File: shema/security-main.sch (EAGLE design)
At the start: 22 parts, among them Q1 IRF520, Q2 FDN360P, T1 2N706, T2 2N706

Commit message: shema changed
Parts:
- removed T1, T2: 2N706, transistor:2N706
- added C3, C4, C5: (no value), capacitor-wima:C2,5-3
- added D4: MBRA340T3, diode:MBRA340T3
- added JP1: (no value), pinhead:PINHD-1X2/90
- added JP2: (no value), adafruit:PINHD-1X8BIG
- added Q3, Q4: AP3310GH, transistor-power:FDN360P
- added SV1: (no value), con-lstb:MA08-1
- renumbered U1 to PIC16F690
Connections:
- removed net N$11: SG1.-, T2.C
- removed net N$4: PIC16F690.RB6/SCK/SCL
- new net DOOR_BUTTON: C4.1, D4.A, PIC16F690.RB6/SCK/SCL
- new net N$1: D4.C, X1-3.KL
- new net N$2: Q4.D, SG1.+
- net DOOR: now also C3.1, Q3.D; no longer T1.E
- net GND: now also C3.2, C4.2, C5.2, JP1.2, SG1.-; no longer T2.E
- net KEYPAD_COL1: now also JP2.5, SV1.5
- net KEYPAD_COL2: now also JP2.6, SV1.6
- net KEYPAD_COL3: now also JP2.7, SV1.7
- net KEYPAD_COL4: now also JP2.8, SV1.8
- net KEYPAD_ROW1: now also JP2.1, SV1.1
- net KEYPAD_ROW2: now also JP2.2, SV1.2
- net KEYPAD_ROW3: now also JP2.3, SV1.3
- net KEYPAD_ROW4: now also JP2.4, SV1.4
- net N$12: now also Q3.G; no longer T1.B
- net N$3: now also Q4.G; no longer T2.B
- net V+: now also C5.1, JP1.1, Q3.S, Q4.S; no longer SG1.+, T1.C
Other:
- moved on the sheet: C1, C2, KEYPAD4X4, LED1, LED2, Q1, Q2, R1, R2, R3, R4, SG1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

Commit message: sheme changes
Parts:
- removed Q3, Q4: AP3310GH, transistor-power:FDN360P
- removed X2: (no value), con-ptr500:AK300/3
- removed X3: (no value), con-ptr500:AK300/5
- removed X4: (no value), con-ptr500:AK300/2
- added C6: 0.1, capacitor-wima:C2,5-3
- added C7: 1500x6.3, rcl:CPOL-EU153CLV-0505
- added C8: 0.047, capacitor-wima:C2,5-3
- added D5: MBRA340T3, diode:MBRA340T3
- added JP3: PICkit2, pinhead:PINHD-1X5
- added JP4: SPI, pinhead:PINHD-1X4
- added JP5: RS-232, adafruit:PINHD-1X3
- added R5, R6: 10k, resistor:R-EU_0204/2V
- added S1, S2: RDT1034, switch:RDT1034
- C1, C2, C3, C4: value (none) -> 10n
- C5: value (none) -> 0.1
- JP1: value (none) -> POWER
- JP2: device adafruit:PINHD-1X8BIG -> adafruit:PINHD-1X8CLEANBIG
- LED1: value W49180 -> FLY-5013GD
- LED2: value W49180 -> FLY-5013SRD
- PIC16F690: value (none) -> CPU
- Q1: value IRF520 -> 70TO3GH; device transistor-power:IRF520 -> adafruit:MOSFET-NREFLOW
- Q2: value FDN360P -> 2N4403; device transistor-power:FDN360P -> transistor-pnp:MPSA56-TO92
- R1, R4: value (none) -> 1K
- R2, R3: value (none) -> 1k
- SG1: value EB2209A -> KPX-1205A
- SV1: value (none) -> KEYPAD
- X1: value (none) -> DOOR-SENSORS
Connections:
- net N$1 renamed DOOR_BUTTON-1
- net N$5 renamed DOOR-1
- net N$6 renamed LOOK2-1
- net N$7 renamed LOOK1-1
- removed net KEYPAD_COL4: JP2.8, KEYPAD4X4.C4, PIC16F690.RA3/MCLR/VPP, SV1.8
- removed net KEYPAD_ROW4: JP2.4, KEYPAD4X4.R4, PIC16F690.AN7/RC3, SV1.4
- removed net LOOK1: C1.1, D1.A, PIC16F690.RA4/AN3/T1GI/OSC2
- removed net LOOK2: C2.1, D2.A, PIC16F690.RA5/T1CKI/OSC1
- removed net N$3 (its old number): Q4.G, R2.2
- new net ICSPCLK: JP3.5
- new net ICSPDAT: JP3.4
- new net KEYPAD_COL1-1: JP2.4, KEYPAD4X4.C1
- new net KEYPAD_COL2-1: JP2.3, KEYPAD4X4.C2
- new net KEYPAD_COL3-1: JP2.2, KEYPAD4X4.C3
- new net KEYPAD_COL4-1: JP2.1, KEYPAD4X4.C4
- new net KEYPAD_ROW1-1: JP2.8, KEYPAD4X4.R1
- new net KEYPAD_ROW2-1: JP2.7, KEYPAD4X4.R2
- new net KEYPAD_ROW3-1: JP2.6, KEYPAD4X4.R3
- new net KEYPAD_ROW4-1: JP2.5, KEYPAD4X4.R4
- new net LOOCK1: C3.1, D1.A, PIC16F690.RA4/AN3/T1GI/OSC2
- new net LOOCK2: C1.1, D2.A, PIC16F690.RA5/T1CKI/OSC1
- new net N$1: Q1.G, R2.2
- new net N$4: D5.A, JP1.1
- new net RESET: PIC16F690.RA3/MCLR/VPP, S2.B
- new net SCK: JP4.3, PIC16F690.RB6/SCK/SCL
- new net SDI: JP4.1, PIC16F690.RB4/AN10/SDI/SDO
- new net SDO: JP4.2, PIC16F690.AN9/RC7
- new net VDD_TARGET: JP3.2
- new net VPP: JP3.1
- new net VSS_GROUND: JP3.3
- net BUZ: now also PIC16F690.RC4; no longer PIC16F690.RC5
- net DOOR: now also C4.1, PIC16F690.AN7/RC3, R5.1; no longer C3.1, PIC16F690.RB4/AN10/SDI/SDO, Q3.D, X1-5.KL
- net DOOR-LEDS: now also PIC16F690.RC5; no longer PIC16F690.RC4
- net DOOR_BUTTON: now also C2.1, PIC16F690.AN8/RC6, R6.1, S1.B; no longer C4.1, PIC16F690.RB6/SCK/SCL
- net GND: now also C6.2, C7.-, C8.1, JP4.4, JP5.3, Q1.S, S1.A1, S2.A1; no longer SG1.-, X2-3.KL, X4-1.KL
- net KEYPAD_COL1: no longer JP2.5, KEYPAD4X4.C1
- net KEYPAD_COL2: no longer JP2.6, KEYPAD4X4.C2
- net KEYPAD_COL3: no longer JP2.7, KEYPAD4X4.C3
- net KEYPAD_ROW1: no longer JP2.1, KEYPAD4X4.R1
- net KEYPAD_ROW2: no longer JP2.2, KEYPAD4X4.R2
- net KEYPAD_ROW3: no longer JP2.3, KEYPAD4X4.R3
- net LED-SYS1: now also R1.1; no longer PIC16F690.AN8/RC6, R4.1
- net LED-SYS2: now also Q2.C, R4.1, X1-5.KL; no longer PIC16F690.AN9/RC7, R1.1
- net N$12: now also Q2.B; no longer Q3.G
- net N$2: now also Q1.D, SG1.-; no longer Q4.D, SG1.+
- net RX: now also JP5.1; no longer X2-1.KL
- net TX: now also JP5.2; no longer X2-2.KL
- net V+: now also C6.1, C7.+, C8.2, D5.C, Q2.E, R5.2, R6.2, SG1.+; no longer JP1.1, Q3.S, Q4.S, X4-2.KL
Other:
- note added: "DOOR"
- note added: "DOOR BUTTON"
- note added: "DOOR LEDS"
- note added: "GND"
- note added: "LOOK1"
- note added: "LOOK2"
- moved on the sheet: C1, C2, C3, C4, C5, JP1, JP2, LED1, LED2, R1, R2, R4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

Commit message: changed sheme
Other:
- note added: "LOOCK1"
- note added: "LOOCK2"
- note added: "Security Alarm https://github.com/lexxai/SecurityAlarm http://lexxai.pp.ua 2017"
- note removed: "LOOK1"
- note removed: "LOOK2"
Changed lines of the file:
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@@
 <sheet>
 <plain>
-<text x="-34.798" y="34.798" size="1.778" layer="91">LOOK1</text>
-<text x="-34.798" y="29.972" size="1.778" layer="91">LOOK2</text>
+<text x="-34.798" y="34.798" size="1.778" layer="91">LOOCK1</text>
+<text x="-34.798" y="29.972" size="1.778" layer="91">LOOCK2</text>
 <text x="-27.178" y="19.558" size="1.778" layer="91" align="bottom-right">DOOR</text>
 <text x="-27.178" y="14.478" size="1.778" layer="91" align="bottom-right">DOOR LEDS</text>
 <text x="-27.178" y="24.892" size="1.778" layer="91" align="bottom-right">DOOR BUTTON</text>
 <text x="-27.178" y="9.652" size="1.778" layer="91" align="bottom-right">GND</text>
+<text x="99.06" y="101.6" size="1.778" layer="91">Security Alarm
+https://github.com/lexxai/SecurityAlarm
+http://lexxai.pp.ua
+2017</text>
 </plain>
 <instances>
@@
 </segment>
 </net>
+<net name="N$5" class="0">
+<segment>
+<wire x1="96.52" y1="114.3" x2="96.52" y2="99.06" width="0.1524" layer="91"/>
+<wire x1="96.52" y1="99.06" x2="144.78" y2="99.06" width="0.1524" layer="91"/>
+<wire x1="144.78" y1="99.06" x2="144.78" y2="114.3" width="0.1524" layer="91"/>
+<wire x1="144.78" y1="114.3" x2="96.52" y2="114.3" width="0.1524" layer="91"/>
+</segment>
+</net>
+<net name="N$6" class="0">
+<segment>
+<wire x1="-45.72" y1="124.46" x2="-45.72" y2="-25.4" width="0.1524" layer="91"/>
+<wire x1="-45.72" y1="-25.4" x2="190.5" y2="-25.4" width="0.1524" layer="91"/>
+<wire x1="190.5" y1="-25.4" x2="190.5" y2="124.46" width="0.1524" layer="91"/>
+<wire x1="190.5" y1="124.46" x2="-45.72" y2="124.46" width="0.1524" layer="91"/>
+</segment>
+</net>
 </nets>
 </sheet>
@@
 </schematic>
 </drawing>
+<compatibility>
+<note version="6.3" minversion="6.2.2" severity="warning">
+Since Version 6.2.2 text objects can contain more than one line,
+which will not be processed correctly with this version.
+</note>
+</compatibility>
 </eagle>

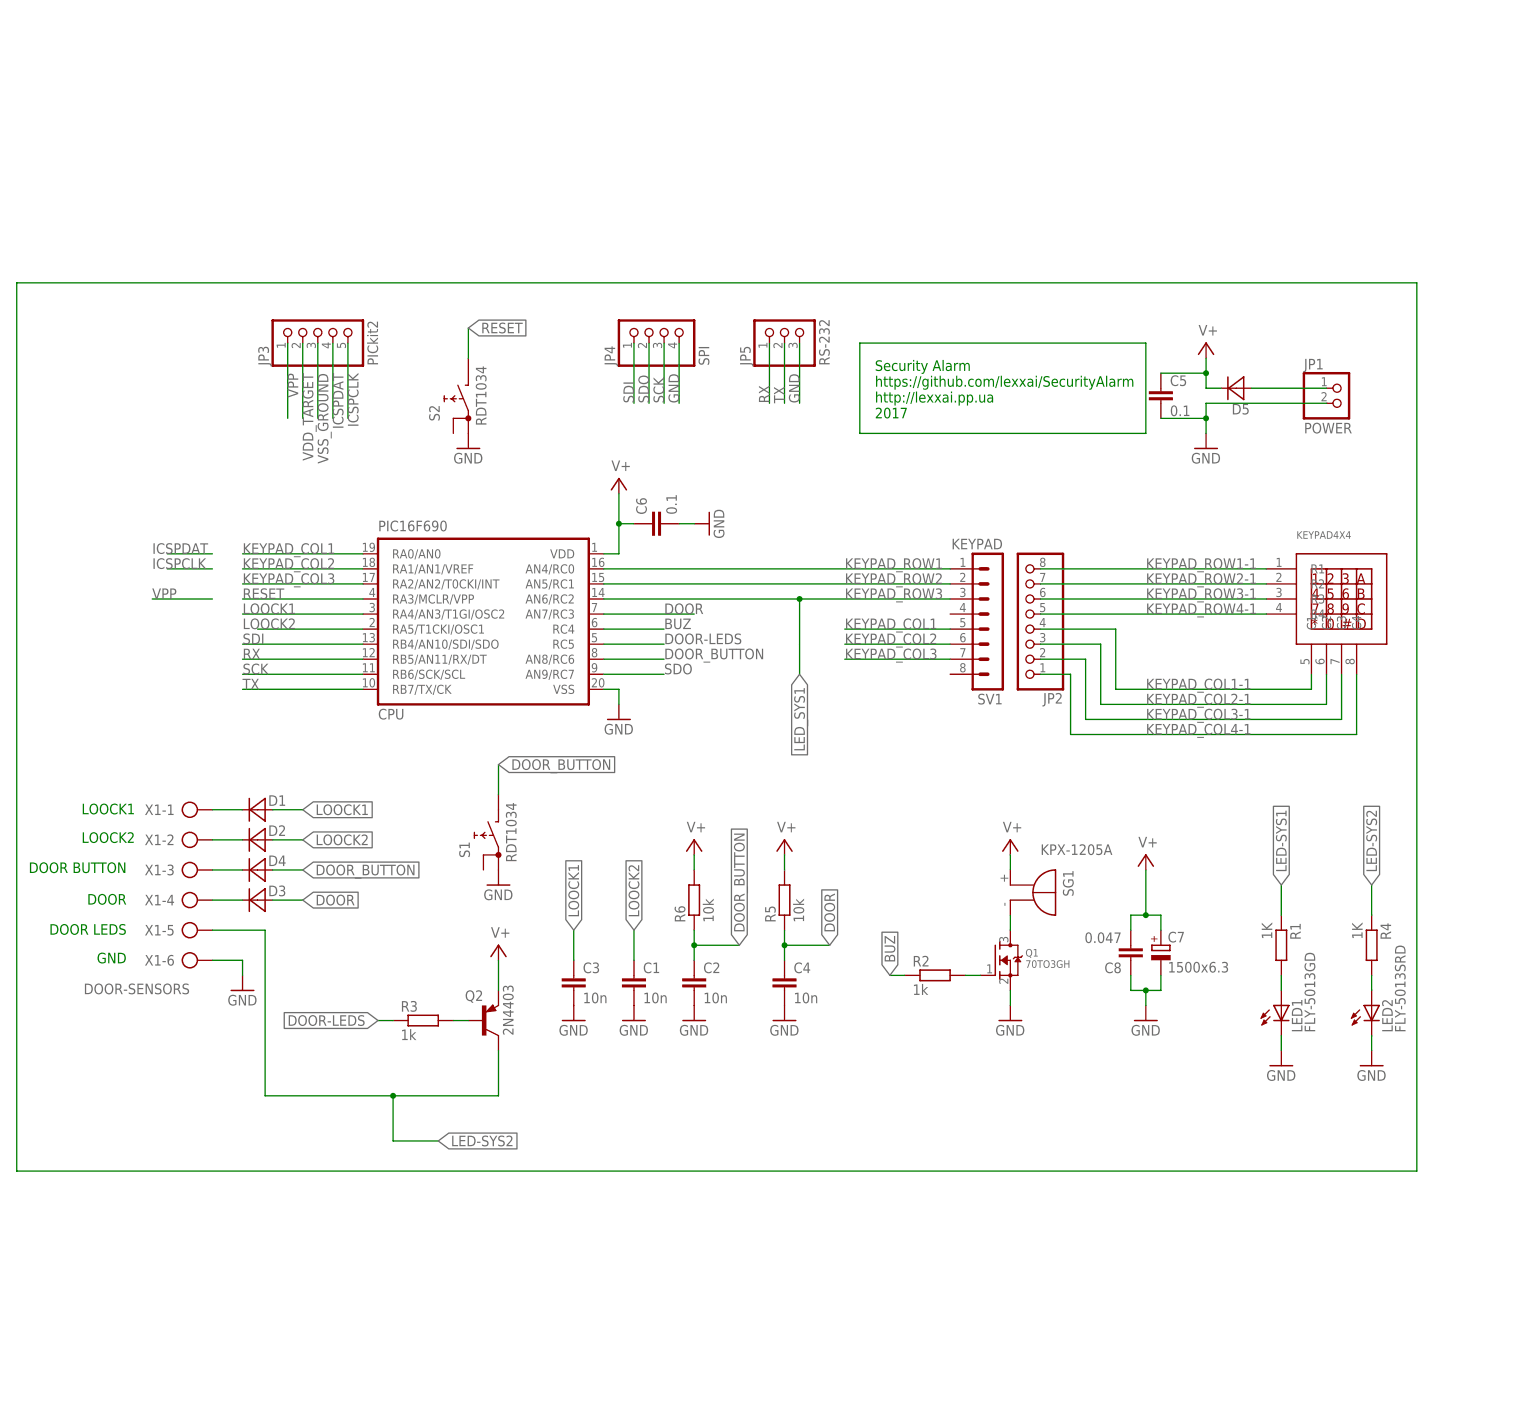
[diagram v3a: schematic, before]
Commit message: 1wire lib added , not tested shema changes: power supply
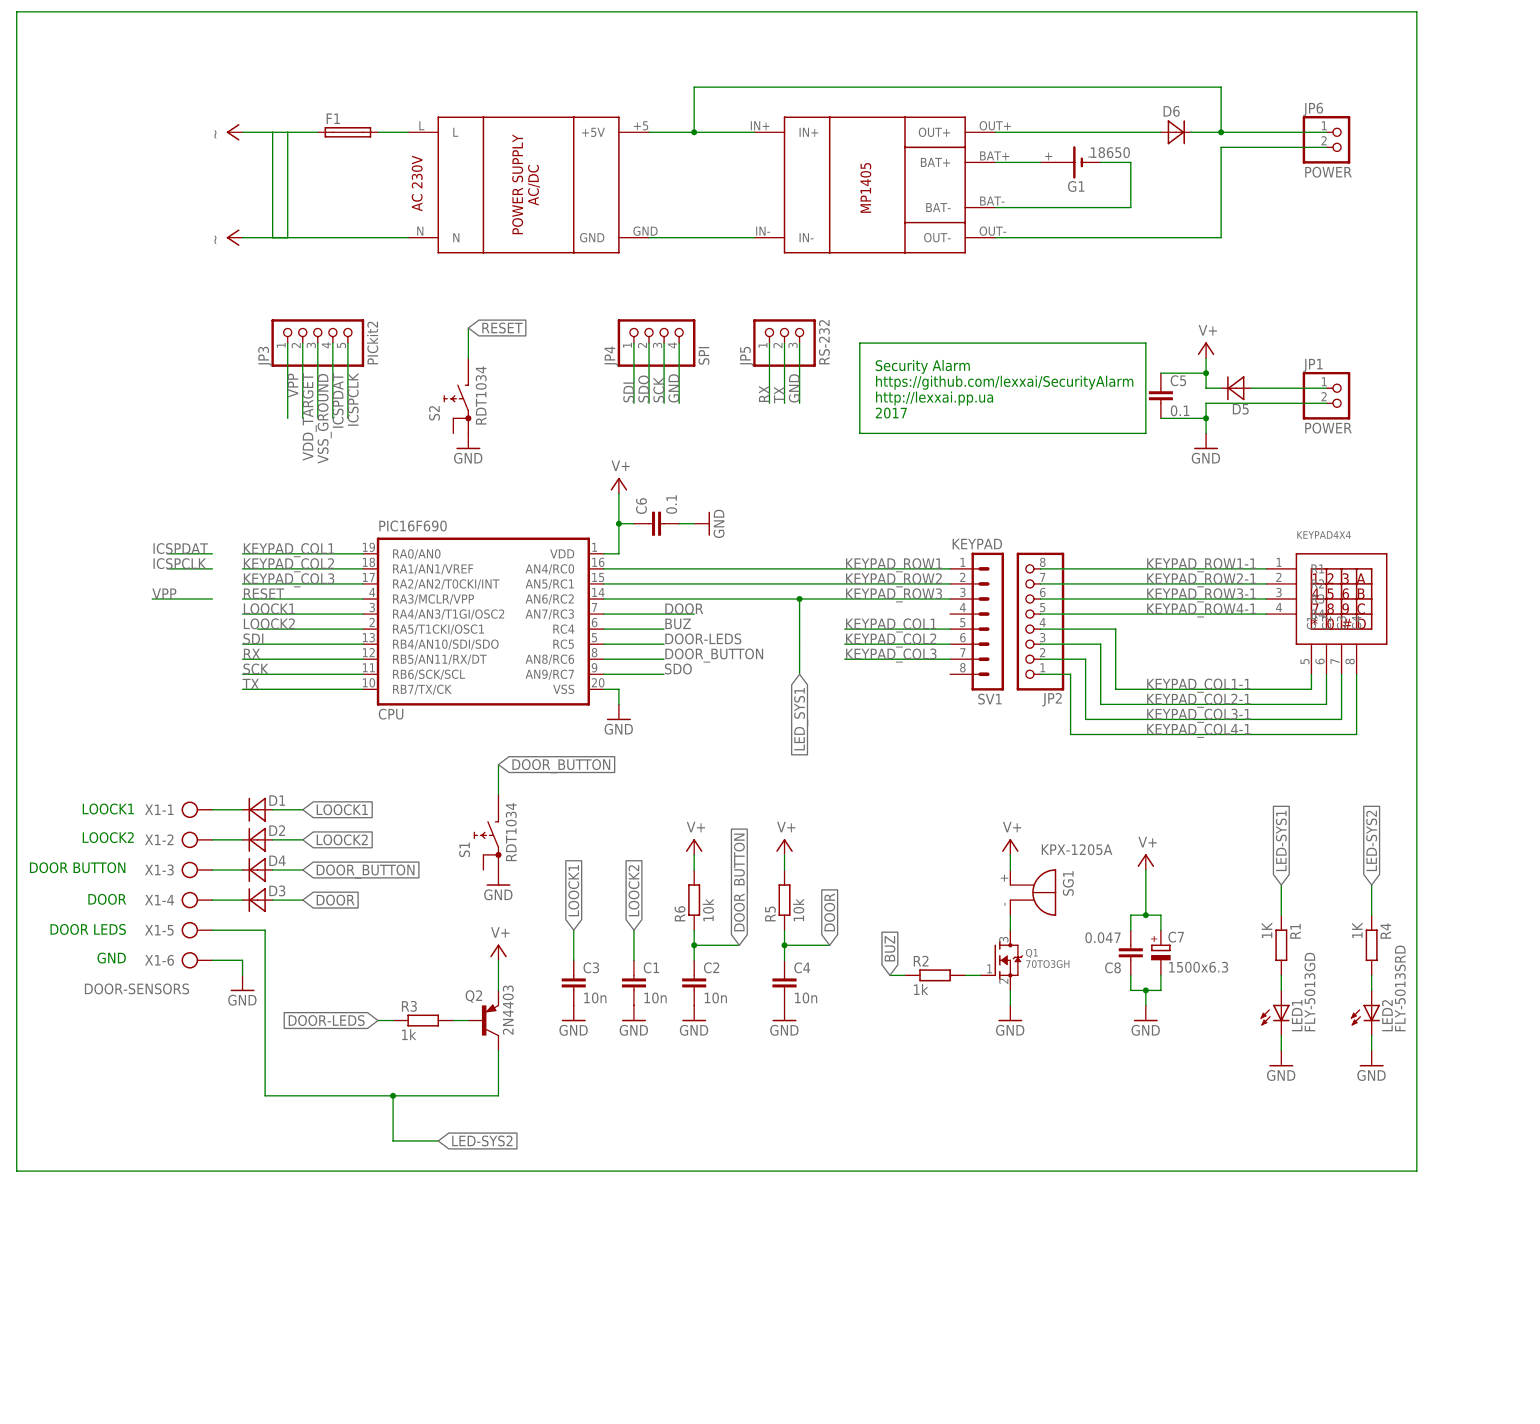
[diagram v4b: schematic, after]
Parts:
- added D6: MBRA340T3, diode:MBRA340T3
- added F1: (no value), fuse:TE5
- added G1: 18650, battery:CRAA
- added JP6: POWER, pinhead:PINHD-1X2/90
- added U$1: POWER_CHARGER+5PS1, lex-library:POWER_CHARGER+5PS1
- added U$2: (no value), lex-library:MP1405
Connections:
- new net N$10: U$1.GND, U$2.IN-
- new net N$11: D6.A, U$2.OUT+
- new net N$13: JP6.2, U$2.OUT-
- new net N$16: F1.2, U$1.L
- new net N$17: U$1.N
- new net N$18: F1.1
- new net N$7: G1.+, U$2.BAT+
- new net N$8: G1.-, U$2.BAT-
- new net N$9: D6.C, JP6.1, U$1.+5V, U$2.IN+
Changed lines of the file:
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@@
 <part name="S2" library="switch" deviceset="RDT1034" device=""/>
 <part name="GND16" library="supply1" deviceset="GND" device=""/>
+<part name="U$1" library="lex-library" deviceset="POWER_CHARGER+5" device="PS1"/>
+<part name="U$2" library="lex-library" deviceset="MP1405" device=""/>
+<part name="G1" library="battery" deviceset="CRAA" device="" value="18650"/>
+<part name="D6" library="diode" deviceset="MBRA340T3" device="" value=""/>
+<part name="JP6" library="pinhead" deviceset="PINHD-1X2" device="/90" value="POWER"/>
+<part name="F1" library="fuse" deviceset="TE5" device=""/>
+<part name="SUPPLY1" library="supply2" deviceset="V+" device="" value="~"/>
+<part name="SUPPLY2" library="supply2" deviceset="V+" device="" value="~"/>
 </parts>
 <sheets>
@@
 <instance part="S2" gate="G$1" x="27.94" y="104.14" rot="R90"/>
 <instance part="GND16" gate="1" x="30.48" y="96.52"/>
+<instance part="U$1" gate="G$1" x="22.86" y="134.62" rot="MR0"/>
+<instance part="U$2" gate="G$1" x="116.84" y="134.62"/>
+<instance part="G1" gate="G$1" x="132.08" y="144.78" smashed="yes" rot="R180">
+<attribute name="NAME" x="134.62" y="141.605" size="1.778" layer="95" rot="R180"/>
+<attribute name="VALUE" x="142.24" y="147.32" size="1.778" layer="96" rot="R180"/>
+</instance>
+<instance part="D6" gate="G$1" x="149.86" y="149.86"/>
+<instance part="JP6" gate="G$1" x="177.8" y="147.32"/>
+<instance part="F1" gate="1" x="10.16" y="149.86"/>
+<instance part="SUPPLY1" gate="1" x="-10.16" y="149.86" rot="R90"/>
+<instance part="SUPPLY2" gate="1" x="-10.16" y="132.08" rot="R90"/>
 </instances>
 <busses>
@@
 <net name="N$6" class="0">
 <segment>
-<wire x1="-45.72" y1="124.46" x2="-45.72" y2="-25.4" width="0.1524" layer="91"/>
+<wire x1="-45.72" y1="170.18" x2="-45.72" y2="-25.4" width="0.1524" layer="91"/>
 <wire x1="-45.72" y1="-25.4" x2="190.5" y2="-25.4" width="0.1524" layer="91"/>
-<wire x1="190.5" y1="-25.4" x2="190.5" y2="124.46" width="0.1524" layer="91"/>
-<wire x1="190.5" y1="124.46" x2="-45.72" y2="124.46" width="0.1524" layer="91"/>
-</segment>
-</net>
+<wire x1="190.5" y1="-25.4" x2="190.5" y2="170.18" width="0.1524" layer="91"/>
+<wire x1="190.5" y1="170.18" x2="-45.72" y2="170.18" width="0.1524" layer="91"/>
+</segment>
+</net>
+<net name="N$7" class="0">
+<segment>
+<pinref part="U$2" gate="G$1" pin="BAT+"/>
+<pinref part="G1" gate="G$1" pin="+"/>
+<wire x1="119.38" y1="144.78" x2="127" y2="144.78" width="0.1524" layer="91"/>
+</segment>
+</net>
+<net name="N$8" class="0">
+<segment>
+<pinref part="G1" gate="G$1" pin="-"/>
+<wire x1="137.16" y1="144.78" x2="142.24" y2="144.78" width="0.1524" layer="91"/>
+<wire x1="142.24" y1="144.78" x2="142.24" y2="137.16" width="0.1524" layer="91"/>
+<pinref part="U$2" gate="G$1" pin="BAT-"/>
+<wire x1="142.24" y1="137.16" x2="119.38" y2="137.16" width="0.1524" layer="91"/>
+</segment>
+</net>
+<net name="N$9" class="0">
+<segment>
+<pinref part="U$1" gate="G$1" pin="+5V"/>
+<pinref part="U$2" gate="G$1" pin="IN+"/>
+<wire x1="60.96" y1="149.86" x2="68.58" y2="149.86" width="0.1524" layer="91"/>
+<wire x1="68.58" y1="149.86" x2="78.74" y2="149.86" width="0.1524" layer="91"/>
+<wire x1="68.58" y1="149.86" x2="68.58" y2="157.48" width="0.1524" layer="91"/>
+<junction x="68.58" y="149.86"/>
+<pinref part="D6" gate="G$1" pin="C"/>
+<wire x1="152.4" y1="149.86" x2="157.48" y2="149.86" width="0.1524" layer="91"/>
+<wire x1="157.48" y1="149.86" x2="175.26" y2="149.86" width="0.1524" layer="91"/>
+<wire x1="68.58" y1="157.48" x2="157.48" y2="157.48" width="0.1524" layer="91"/>
+<wire x1="157.48" y1="157.48" x2="157.48" y2="149.86" width="0.1524" layer="91"/>
+<junction x="157.48" y="149.86"/>
+<pinref part="JP6" gate="G$1" pin="1"/>
+</segment>
+</net>
+<net name="N$10" class="0">
+<segment>
+<pinref part="U$1" gate="G$1" pin="GND"/>
+<pinref part="U$2" gate="G$1" pin="IN-"/>
+<wire x1="60.96" y1="132.08" x2="78.74" y2="132.08" width="0.1524" layer="91"/>
+</segment>
+</net>
+<net name="N$11" class="0">
+<segment>
+<pinref part="U$2" gate="G$1" pin="OUT+"/>
+<wire x1="119.38" y1="149.86" x2="147.32" y2="149.86" width="0.1524" layer="91"/>
+<pinref part="D6" gate="G$1" pin="A"/>
+</segment>
+</net>
+<net name="N$13" class="0">
+<segment>
+<pinref part="U$2" gate="G$1" pin="OUT-"/>
+<wire x1="119.38" y1="132.08" x2="157.48" y2="132.08" width="0.1524" layer="91"/>
+<wire x1="157.48" y1="132.08" x2="157.48" y2="147.32" width="0.1524" layer="91"/>
+<pinref part="JP6" gate="G$1" pin="2"/>
+<wire x1="157.48" y1="147.32" x2="175.26" y2="147.32" width="0.1524" layer="91"/>
+</segment>
+</net>
+<net name="N$16" class="0">
+<segment>
+<pinref part="U$1" gate="G$1" pin="L"/>
+<pinref part="F1" gate="1" pin="2"/>
+<wire x1="20.32" y1="149.86" x2="15.24" y2="149.86" width="0.1524" layer="91"/>
+</segment>
+</net>
+<net name="N$17" class="0">
+<segment>
+<pinref part="U$1" gate="G$1" pin="N"/>
+<wire x1="20.32" y1="132.08" x2="-7.62" y2="132.08" width="0.1524" layer="91"/>
+</segment>
+</net>
+<net name="N$18" class="0">
+<segment>
+<pinref part="F1" gate="1" pin="1"/>
+<wire x1="5.08" y1="149.86" x2="0" y2="149.86" width="0.1524" layer="91"/>
+<wire x1="0" y1="149.86" x2="-2.54" y2="149.86" width="0.1524" layer="91"/>
+<wire x1="-2.54" y1="149.86" x2="-7.62" y2="149.86" width="0.1524" layer="91"/>
+<wire x1="-2.54" y1="149.86" x2="-2.54" y2="132.08" width="0.1524" layer="91"/>
+<wire x1="-2.54" y1="132.08" x2="0" y2="132.08" width="0.1524" layer="91"/>
+<wire x1="0" y1="132.08" x2="0" y2="149.86" width="0.1524" layer="91"/>
+</segment>
+</net>
